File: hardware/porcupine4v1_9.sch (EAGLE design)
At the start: 33 parts, among them X1 PROGCON

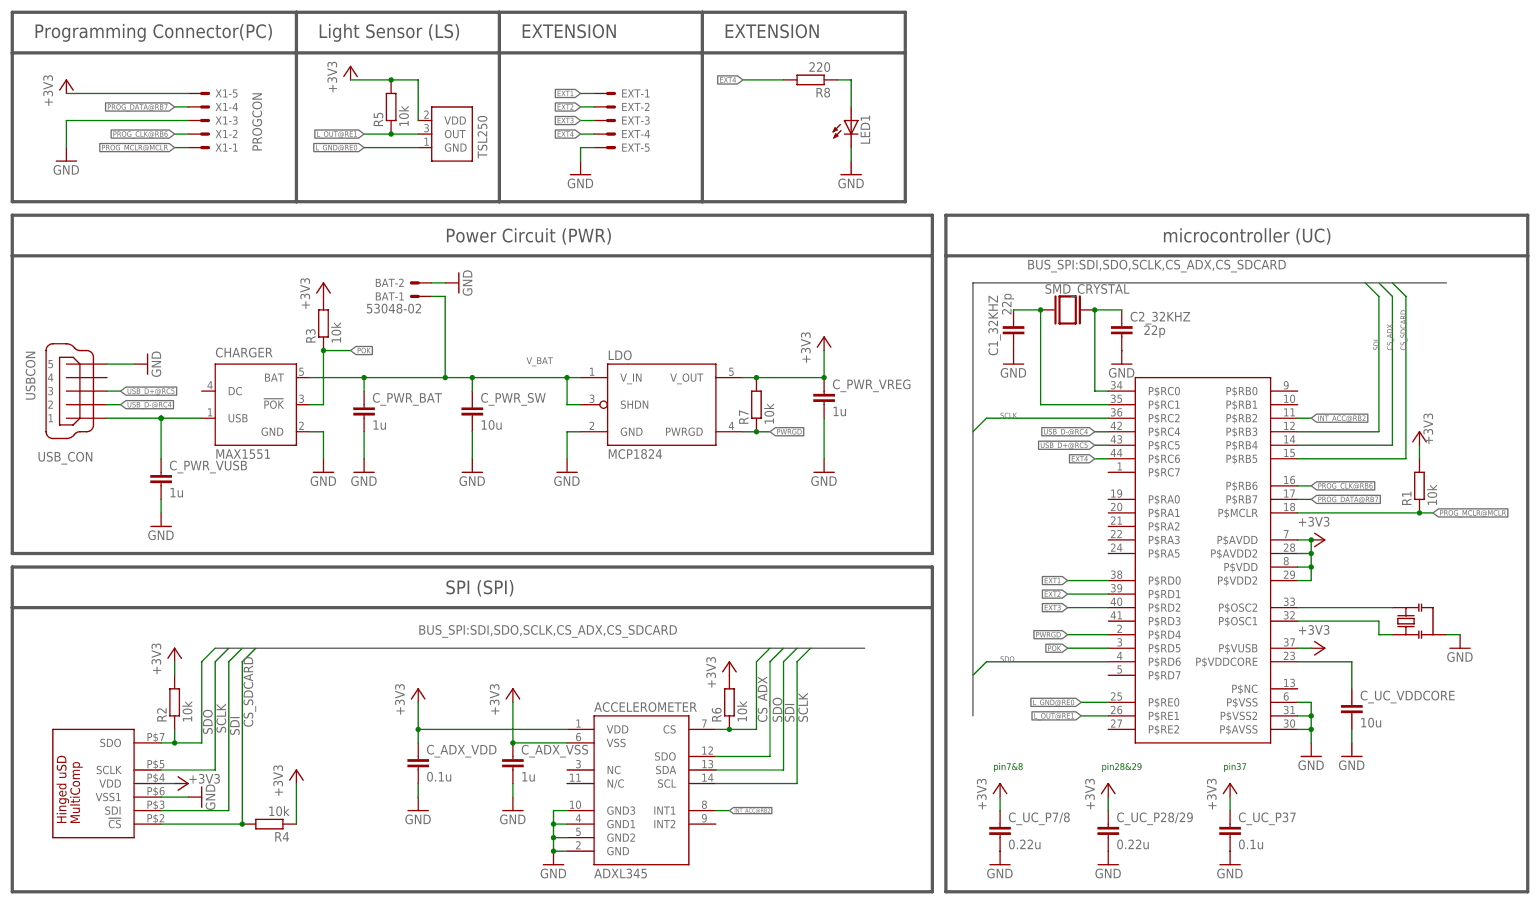
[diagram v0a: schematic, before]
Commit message: updated hedgehog library and next iteration versions
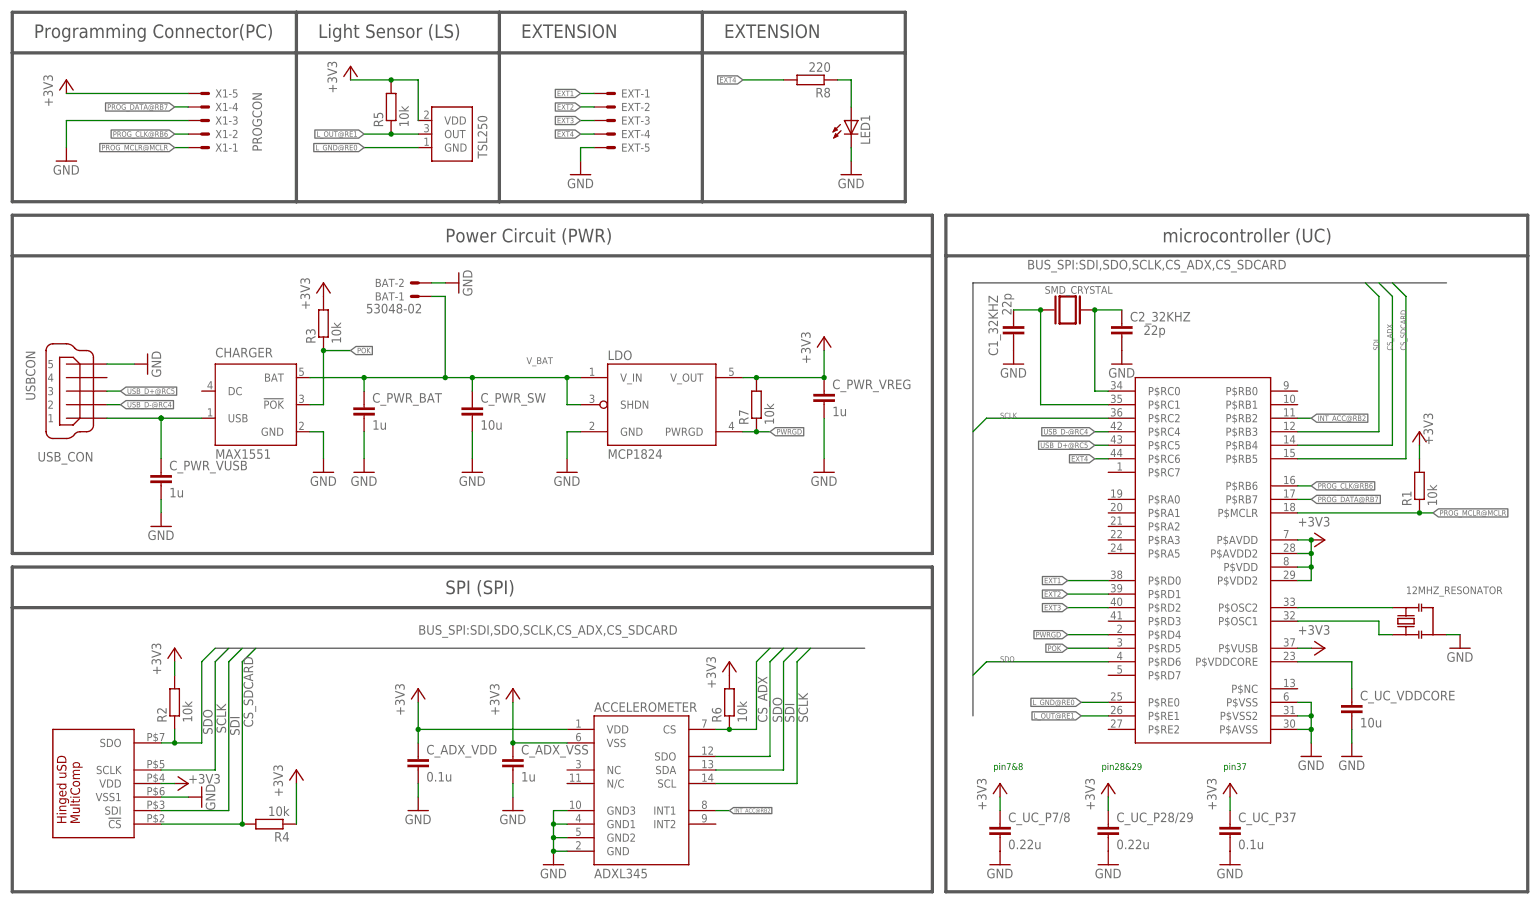
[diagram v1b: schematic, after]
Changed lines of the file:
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@@
 <instances>
 <instance part="GND3" gate="1" x="12.7" y="139.7"/>
-<instance part="SDCARD_CON" gate="G$1" x="30.48" y="25.4" rot="R90"/>
+<instance part="SDCARD_CON" gate="G$1" x="17.78" y="22.86" rot="R90"/>
 <instance part="GND16" gate="1" x="38.1" y="20.32" rot="R90"/>
 <instance part="LIGHTSENSE" gate="G$1" x="83.82" y="144.78" smashed="yes">
@@
 <instance part="GND1" gate="1" x="274.32" y="48.26"/>
 <instance part="32KHZ_CRYSTAL" gate="G$1" x="200.66" y="111.76" smashed="yes">
-<attribute name="VALUE" x="196.342" y="114.808" size="1.778" layer="96"/>
+<attribute name="VALUE" x="196.342" y="114.808" size="1.4224" layer="96"/>
 <attribute name="FARNELL" x="200.66" y="111.76" size="1.778" layer="96" display="off"/>
 </instance>
@@
 <instance part="LED1" gate="G$1" x="160.02" y="147.32"/>
 <instance part="GND10" gate="1" x="109.22" y="137.16"/>
-<instance part="12MHZ_RESONATOR" gate="RESONATOR" x="264.16" y="53.34" rot="R180">
+<instance part="12MHZ_RESONATOR" gate="RESONATOR" x="264.16" y="53.34" smashed="yes" rot="R180">
 <attribute name="DIGIKEY" x="264.16" y="53.34" size="1.778" layer="96" rot="R180" display="off"/>
+<attribute name="NAME" x="264.16" y="58.42" size="1.4224" layer="95"/>
 </instance>
 </instances>
